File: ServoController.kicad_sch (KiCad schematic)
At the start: 13 parts, among them U1 PCA9685PW,118

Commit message: Poprawa
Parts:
- removed R21, R22: 10kΩ, PCM_JLCPCB:R_0402, symbol PCM_JLCPCB-Resistors:0402,10kΩ
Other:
- note removed: "I2C Bus Connection"

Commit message: polished the schemtic
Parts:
- removed D4: LED, LED_SMD:LED_0603_1608Metric, symbol Device:LED
- removed H11, H12, H13, H14, H15, H16: Header-Male-2.54_1x3, easyeda2kicad:HDR-TH_3P-P2.54-V-M-1, symbol SymboleEasyeda2kicad:Header-Male-2.54_1x3
- removed R23: 330Ω, PCM_JLCPCB:R_0402, symbol PCM_JLCPCB-Resistors:0402,330Ω
- added D6, D7: Red, PCM_JLCPCB:D_0603, symbol PCM_JLCPCB-Diodes:LED,0603,Red
- added J10, J11, J6, J7, J8, J9: Conn_01x03, Connector_JST:JST_XH_S3B-XH-A_1x03_P2.50mm_Horizontal, symbol Connector_Generic:Conn_01x03
- added R10, R11: 510Ω, PCM_JLCPCB:R_0402, symbol PCM_JLCPCB-Resistors:0402,510Ω
- added R23, R24, R25, R26, R27, R28, R29, R30, R31, R32, R33, R34: 10kΩ, PCM_JLCPCB:R_0402, symbol PCM_JLCPCB-Resistors:0402,10kΩ
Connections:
- net SEL2 is gone; now on net GND: U1.23 (~{OE})
- net GND: now also D6.1, D7.1, J10.1 (Pin_1), J11.1 (Pin_1), J6.1 (Pin_1), J7.1 (Pin_1), J8.1 (Pin_1), J9.1 (Pin_1), R23.2, R24.2, R25.2, R26.2, R27.2, R34.2; no longer U1.1 (A0), U1.2 (A1), U1.24 (A5), U1.3 (A2), U1.4 (A3), U1.5 (A4)
- net S1: now also J10.2 (Pin_2)
- net S2: now also J9.2 (Pin_2)
- net S3: now also J8.2 (Pin_2)
- net S4: now also J7.2 (Pin_2)
- net S5: now also J6.2 (Pin_2)
- net S6: now also J11.2 (Pin_2)
- net S15: now reaches U1.21 (LED14)
- net S15: now also R11.1
- net S16: now reaches U1.22 (LED15)
- net S16: now also R10.1
- net +5V renamed +3V3
- net +3V3: now also R28.1, R29.1, R30.1, R31.1, R32.1, R33.1
- net U_reg renamed Servo_VCC
- net Servo_VCC: now also J10.3 (Pin_3), J11.3 (Pin_3), J6.3 (Pin_3), J7.3 (Pin_3), J8.3 (Pin_3), J9.3 (Pin_3)
- new net: D6.2, R11.2
- new net: D7.2, R10.2
- new net A0: R33.2, R34.1, U1.1 (A0)
- new net A1: R27.1, R32.2, U1.2 (A1)
- new net A2: R26.1, R31.2, U1.3 (A2)
- new net A3: R23.1, R28.2, U1.4 (A3)
- new net A4: R24.1, R29.2, U1.5 (A4)
- new net A5: R25.1, R30.2, U1.24 (A5)
- no-connect marks 0 -> 8
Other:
- note added: "ADD I2C LEVEL SHIFER TO 5V"
- note added: "Connectors"
- note added: "I2C address select"
- note added: "PWM Generator"
- note added: "Sanity LED's"
- note removed: "'Selected' indicator"
- moved on the sheet: C29, U1

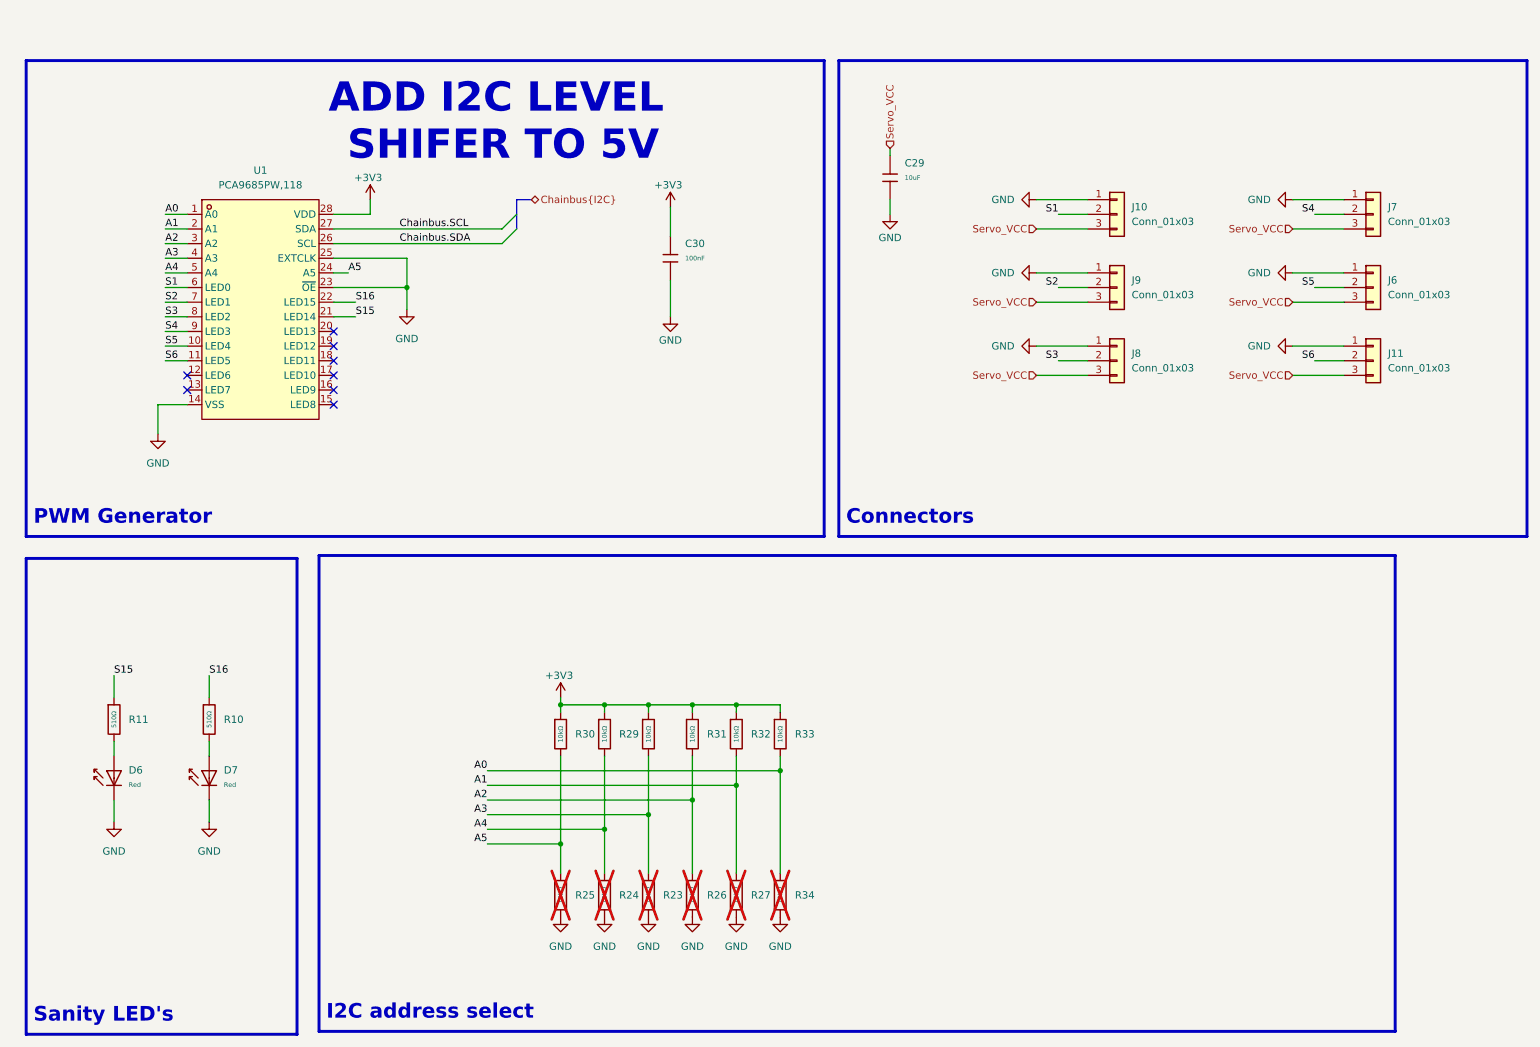
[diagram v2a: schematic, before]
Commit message: added 5V i2c shifter
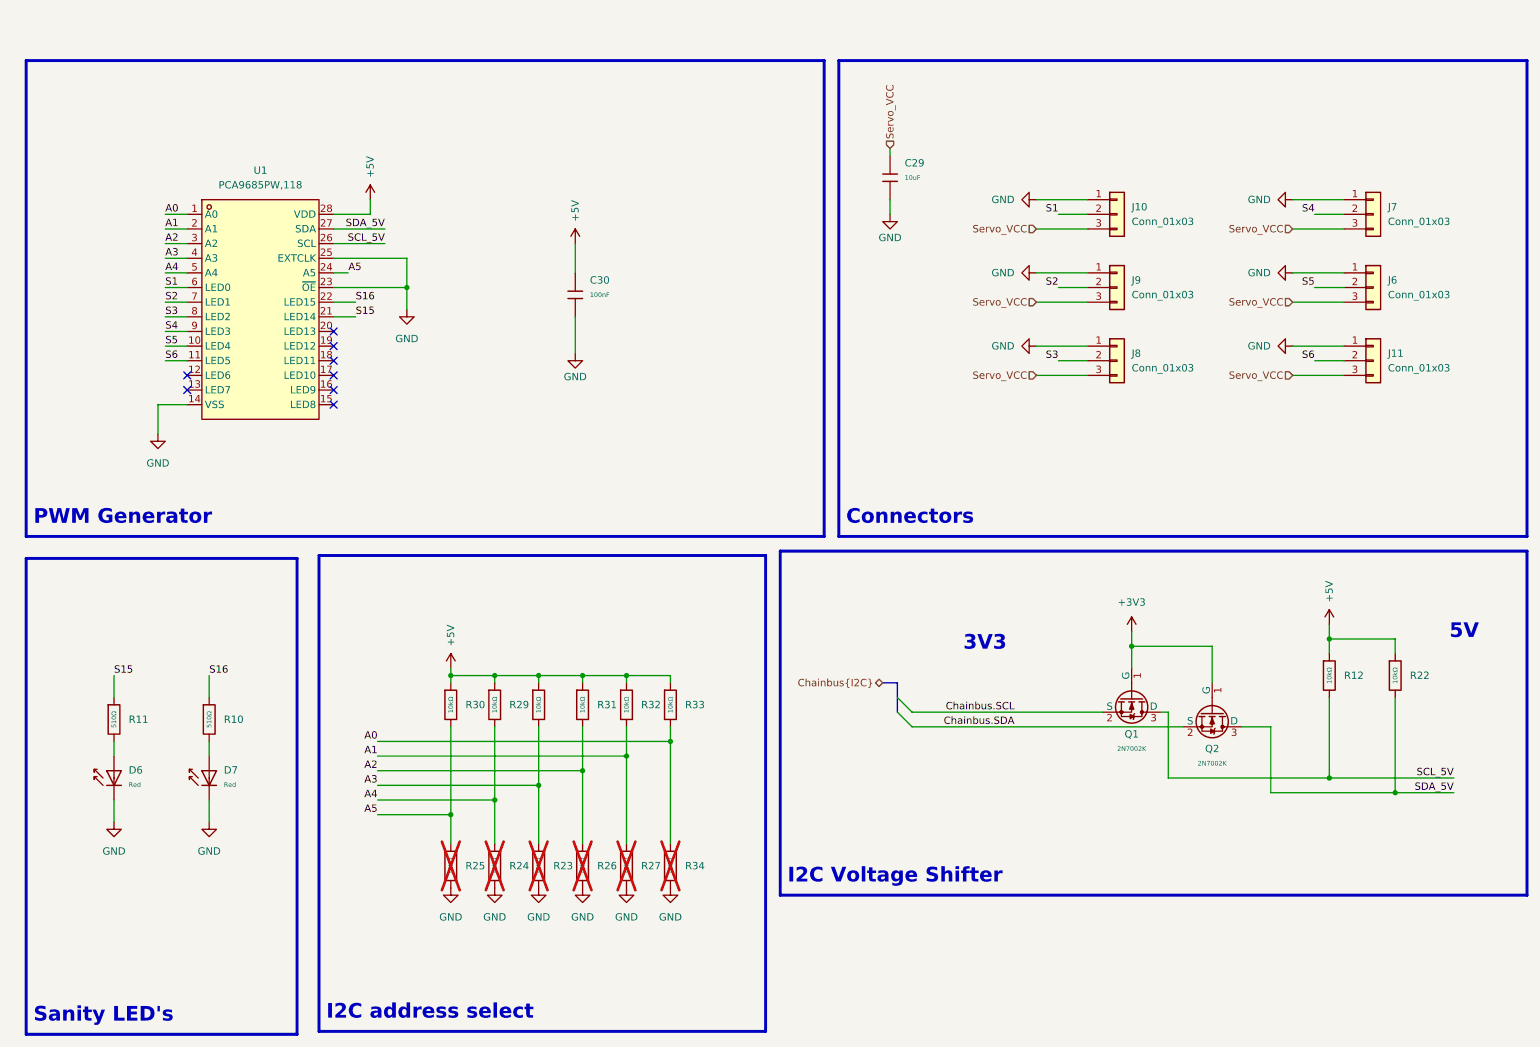
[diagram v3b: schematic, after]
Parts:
- added Q1, Q2: 2N7002K, PCM_JLCPCB:Q_SOT-23, symbol PCM_JLCPCB-Transistors:NMOS,2N7002K
- added R12, R22: 10kΩ, PCM_JLCPCB:R_0402, symbol PCM_JLCPCB-Resistors:0402,10kΩ
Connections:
- net +3V3: now also Q1.1 (G), Q2.1 (G); no longer C30.1, R28.1, R29.1, R30.1, R31.1, R32.1, R33.1, U1.28 (VDD)
- net Chainbus.SCL: now also Q1.2 (S); no longer U1.27 (SDA)
- net Chainbus.SDA: now also Q2.2 (S); no longer U1.26 (SCL)
- new net +5V: C30.1, R12.1, R22.1, R28.1, R29.1, R30.1, R31.1, R32.1, R33.1, U1.28 (VDD)
- new net SCL_5V: Q1.3 (D), R12.2, U1.26 (SCL)
- new net SDA_5V: Q2.3 (D), R22.2, U1.27 (SDA)
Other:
- note added: "3V3"
- note added: "5V"
- note added: "I2C Voltage Shifter"
- note removed: "ADD I2C LEVEL SHIFER TO 5V"
- moved on the sheet: C30, R23, R24, R25, R26, R27, R29, R30, R31, R32, R33, R34

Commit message: PCB design
In progress
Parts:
- removed J11, J6: Conn_01x03, Connector_JST:JST_XH_S3B-XH-A_1x03_P2.50mm_Horizontal, symbol Connector_Generic:Conn_01x03
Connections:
- net S5: no longer names the net of U1.10 (LED4)
- net S6: no longer names the net of U1.11 (LED5)
- no-connect marks 8 -> 10
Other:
- title: (none) -> MMS3 Hat servo controller

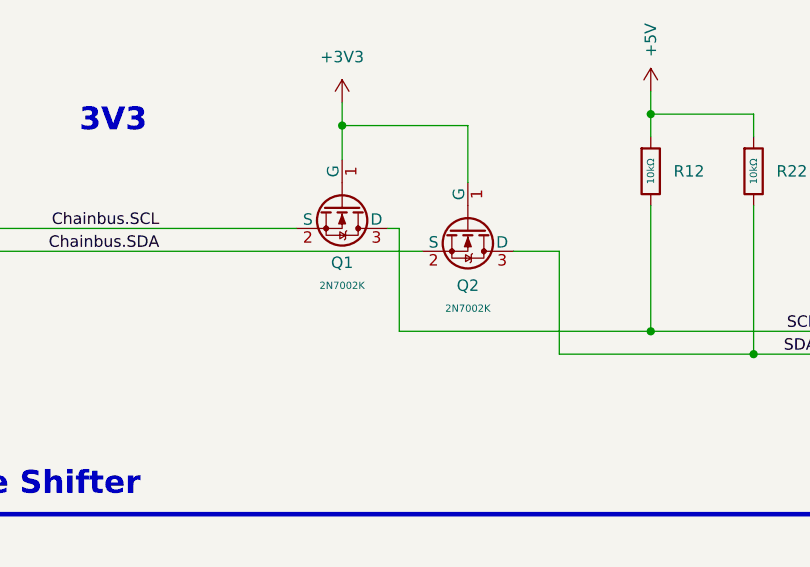
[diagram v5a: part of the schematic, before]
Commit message: change mosfets to basic assembly
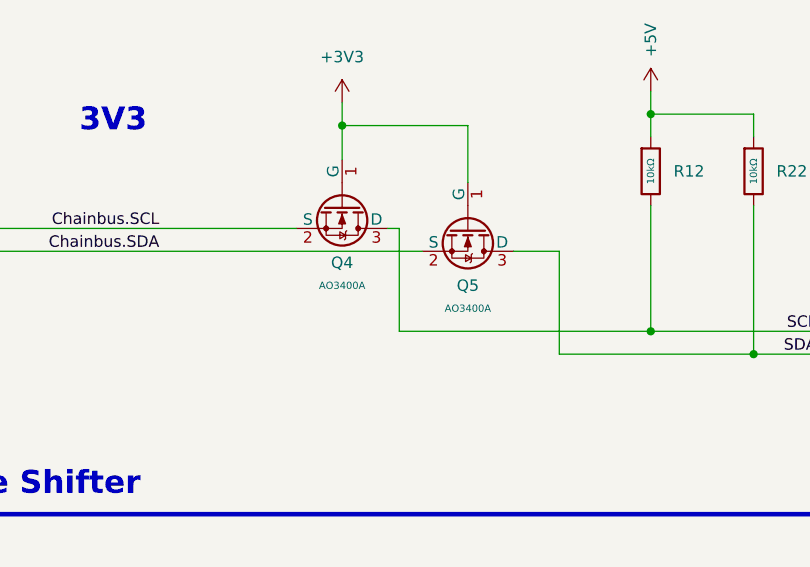
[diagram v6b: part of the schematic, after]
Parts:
- removed Q1, Q2: 2N7002K, PCM_JLCPCB:Q_SOT-23, symbol PCM_JLCPCB-Transistors:NMOS,2N7002K
- added Q4, Q5: AO3400A, PCM_JLCPCB:Q_SOT-23, symbol PCM_JLCPCB-Transistors:NMOS,AO3400A
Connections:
- net +3V3: now also Q4.1 (G), Q5.1 (G)
- net Chainbus.SCL: now also Q4.2 (S)
- net Chainbus.SDA: now also Q5.2 (S)
- net SCL_5V: now also Q4.3 (D)
- net SDA_5V: now also Q5.3 (D)
